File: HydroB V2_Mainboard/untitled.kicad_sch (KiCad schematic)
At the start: 12 parts, among them J3 PH SENSOR, J4 EC SENSOR, U2 SN65HVD72DR

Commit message: Mainboard schematic update
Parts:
- removed D2, D3: LED_Small, LED_SMD:LED_0805_2012Metric, symbol Device:LED_Small
- removed J4: EC SENSOR, Connector_Phoenix_MC:PhoenixContact_MCV_1,5_4-G-3.81_1x04_P3.81mm_Vertical, symbol Connector:Conn_01x04_Pin
- removed R6, R7: 1k, Resistor_SMD:R_0603_1608Metric, symbol Device:R
- added D4: D_TVS, Diode_SMD:D_SOD-123F, symbol Device:D_TVS
- added J1: Conn_01x02_Pin, DC Conn:Modbus, symbol Connector:Conn_01x02_Pin
- added J9: SENSOR, DC Conn:Modbus, symbol Connector:Conn_01x04_Pin
- added TP1, TP2: TestPoint, TestPoint:TestPoint_Loop_D1.80mm_Drill1.0mm_Beaded, symbol Connector:TestPoint
- J3: value PH SENSOR -> SENSOR; footprint Connector_Phoenix_MC:PhoenixContact_MCV_1,5_4-G-3.81_1x04_P3.81mm_Vertical -> DC Conn:Modbus
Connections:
- net +12V: now also J9.4 (Pin_4)
- net GND: now also J9.1 (Pin_1)
- net at R10.2, R11.1, R9.1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: now also J3.3 (Pin_3), D4.1 (A1), J1.1 (Pin_1), J9.3 (Pin_3), TP2.1; no longer J3.2 (Pin_2)
- net at R11.2, R8.1, R9.2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: now also J3.2 (Pin_2), D4.2 (A2), J1.2 (Pin_2), J9.2 (Pin_2), TP1.1; no longer J3.3 (Pin_3)

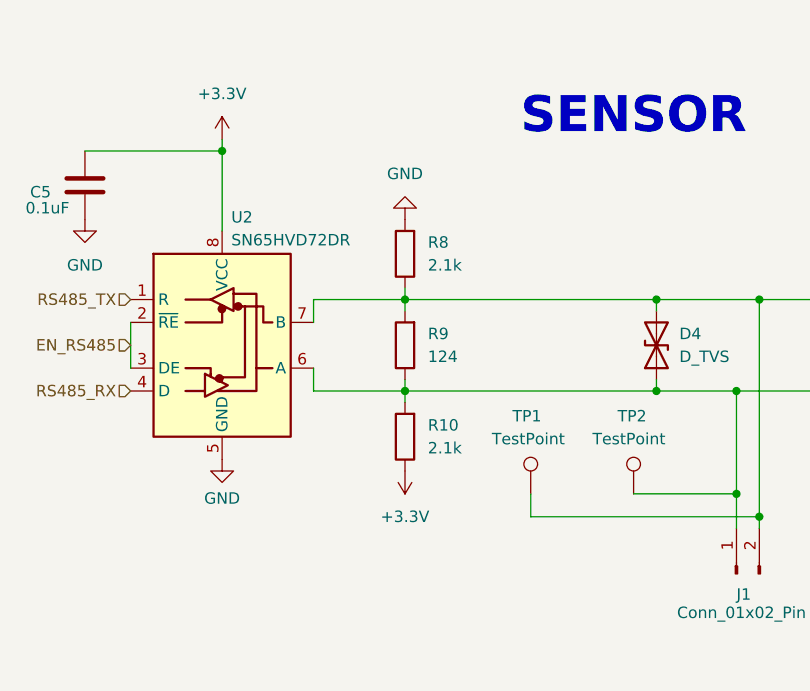
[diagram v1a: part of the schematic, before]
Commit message: main PCB board placement
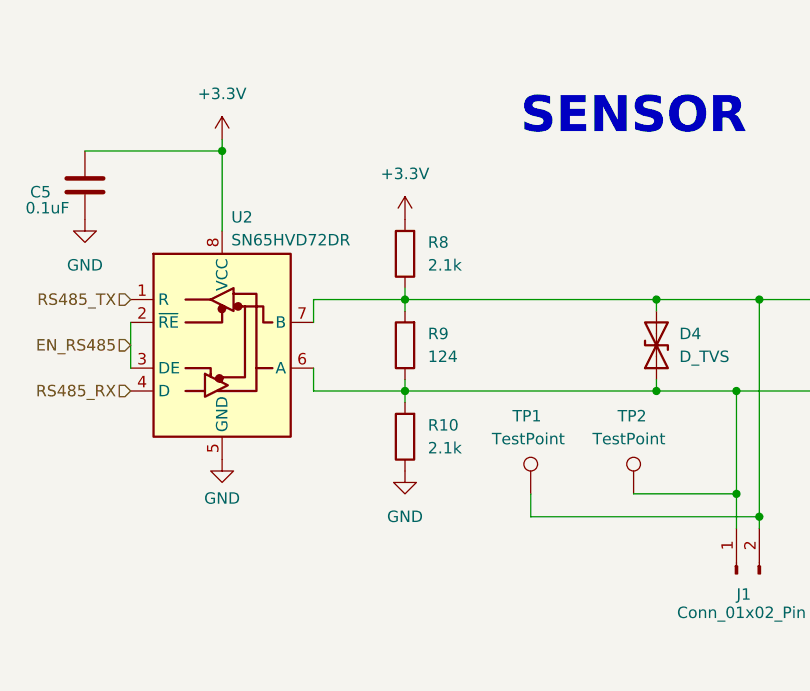
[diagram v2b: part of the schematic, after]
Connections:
- net +3.3V: now also R8.2; no longer R10.1
- net GND: now also R10.1; no longer R8.2
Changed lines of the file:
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@@
 	(symbol
 		(lib_id "power:GND")
-		(at 130.81 85.09 180)
+		(at 130.81 113.03 0)
 		(unit 1)
 		(exclude_from_sim no)
@@
 		(fields_autoplaced yes)
 		(property "Reference" "#PWR017"
-			(at 130.81 78.74 0)
+			(at 130.81 119.38 0)
 			(effects
 				(font
@@
 		)
 		(property "Value" "GND"
-			(at 130.81 80.01 0)
+			(at 130.81 118.11 0)
 			(effects
 				(font
@@
 		)
 		(property "Footprint" ""
-			(at 130.81 85.09 0)
+			(at 130.81 113.03 0)
 			(effects
 				(font
@@
 		)
 		(property "Datasheet" ""
-			(at 130.81 85.09 0)
+			(at 130.81 113.03 0)
 			(effects
 				(font
@@
 		)
 		(property "Description" "Power symbol creates a global label with name \"GND\" , ground"
-			(at 130.81 85.09 0)
+			(at 130.81 113.03 0)
 			(effects
 				(font
@@
 	(symbol
 		(lib_id "power:+3.3V")
-		(at 130.81 113.03 180)
+		(at 130.81 85.09 0)
 		(unit 1)
 		(exclude_from_sim no)
@@
 		(fields_autoplaced yes)
 		(property "Reference" "#PWR018"
-			(at 130.81 109.22 0)
+			(at 130.81 88.9 0)
 			(effects
 				(font
@@
 		)
 		(property "Value" "+3.3V"
-			(at 130.81 118.11 0)
+			(at 130.81 80.01 0)
 			(effects
 				(font
@@
 		)
 		(property "Footprint" ""
-			(at 130.81 113.03 0)
+			(at 130.81 85.09 0)
 			(effects
 				(font
@@
 		)
 		(property "Datasheet" ""
-			(at 130.81 113.03 0)
+			(at 130.81 85.09 0)
 			(effects
 				(font
@@
 		)
 		(property "Description" "Power symbol creates a global label with name \"+3.3V\""
-			(at 130.81 113.03 0)
-			(effects
-				(font
+			(at 130.81 85.09 0)
+			(effects
+				(font

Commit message: PCB placement and ERC
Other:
- company: (none) -> Modbus
- title: (none) -> Prak Chilifong
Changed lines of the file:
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@@
 	(generator_version "8.0")
 	(paper "A4")
+	(title_block
+		(title "Prak Chilifong")
+		(date "2024-10-06")
+		(rev "2.0")
+		(company "Modbus")
+		(comment 1 "Mainboard PCB")
+	)
 	(junction
 		(at 182.88 104.14)
@@
 	)
 	(junction
+		(at 201.93 118.11)
+		(diameter 0)
+		(color 0 0 0 0)
+	)
+	(junction
 		(at 170.18 118.11)
 		(diameter 0)
@@
 	(wire
 		(pts
-			(xy 201.93 115.57) (xy 201.93 119.38)
+			(xy 201.93 115.57) (xy 201.93 118.11)
 		)
 		(stroke
@@
 	(wire
 		(pts
+			(xy 201.93 118.11) (xy 201.93 119.38)
+		)
+		(stroke
+			(width 0)
+			(type default)
+		)
+	)
+	(wire
+		(pts
 			(xy 130.81 92.71) (xy 130.81 93.98)
 		)
@@
 	(wire
 		(pts
+			(xy 212.09 115.57) (xy 212.09 118.11)
+		)
+		(stroke
+			(width 0)
+			(type default)
+		)
+	)
+	(wire
+		(pts
 			(xy 170.18 93.98) (xy 180.34 93.98)
 		)
@@
 	(wire
 		(pts
+			(xy 201.93 118.11) (xy 212.09 118.11)
+		)
+		(stroke
+			(width 0)
+			(type default)
+		)
+	)
+	(wire
+		(pts
 			(xy 100.33 96.52) (xy 100.33 101.6)
 		)
@@
 	(wire
 		(pts
+			(xy 185.42 115.57) (xy 185.42 119.38)
+		)
+		(stroke
+			(width 0)
+			(type default)
+		)
+	)
+	(wire
+		(pts
 			(xy 199.39 104.14) (xy 199.39 119.38)
 		)
@@
 		(pts
 			(xy 158.75 102.87) (xy 158.75 104.14)
-		)
-		(stroke
-			(width 0)
-			(type default)
-		)
-	)
-	(wire
-		(pts
-			(xy 185.42 119.38) (xy 185.42 115.57)
 		)
 		(stroke
@@
 	(text "SENSOR\n"
 		(exclude_from_sim no)
-		(at 156.21 73.66 0)
+		(at 151.384 41.91 0)
 		(effects
 			(font
@@
 	)
 	(symbol
+		(lib_id "power:+12V")
+		(at 201.93 115.57 0)
+		(unit 1)
+		(exclude_from_sim no)
+		(in_bom yes)
+		(on_board yes)
+		(dnp no)
+		(property "Reference" "#PWR025"
+			(at 201.93 119.38 0)
+			(effects
+				(font
+					(size 1.27 1.27)
+				)
+				(hide yes)
+			)
+		)
+		(property "Value" "+12V"
+			(at 201.93 111.506 0)
+			(effects
+				(font
+					(size 1.27 1.27)
+				)
+			)
+		)
+		(property "Footprint" ""
+			(at 201.93 115.57 0)
+			(effects
+				(font
+					(size 1.27 1.27)
+				)
+				(hide yes)
+			)
+		)
+		(property "Datasheet" ""
+			(at 201.93 115.57 0)
+			(effects
+				(font
+					(size 1.27 1.27)
+				)
+				(hide yes)
+			)
+		)
+		(property "Description" "Power symbol creates a global label with name \"+12V\""
+			(at 201.93 115.57 0)
+			(effects
+				(font
+					(size 1.27 1.27)
+				)
+				(hide yes)
+			)
+		)
+		(pin "1"
+		)
+		(instances
+			(project "LCD High Revolution"
+				(path "/7eaed49e-949c-4b32-bb59-42041e199453/cb3a589e-3872-4cde-9770-3d39d4934022/02fbcb66-5250-4d03-96d3-712f7ba2e5b8"
+					(reference "#PWR025")
+					(unit 1)
+				)
+			)
+		)
+	)
+	(symbol
+		(lib_id "power:+12V")
+		(at 185.42 115.57 0)
+		(unit 1)
+		(exclude_from_sim no)
+		(in_bom yes)
+		(on_board yes)
+		(dnp no)
+		(property "Reference" "#PWR020"
+			(at 185.42 119.38 0)
+			(effects
+				(font
+					(size 1.27 1.27)
+				)
+				(hide yes)
+			)
+		)
+		(property "Value" "+12V"
+			(at 185.42 111.76 0)
+			(effects
+				(font
+					(size 1.27 1.27)
+				)
+			)
+		)
+		(property "Footprint" ""
+			(at 185.42 115.57 0)
+			(effects
+				(font
+					(size 1.27 1.27)
+				)
+				(hide yes)
+			)
+		)
+		(property "Datasheet" ""
+			(at 185.42 115.57 0)
+			(effects
+				(font
+					(size 1.27 1.27)
+				)
+				(hide yes)
+			)
+		)
+		(property "Description" "Power symbol creates a global label with name \"+12V\""
+			(at 185.42 115.57 0)
+			(effects
+				(font
+					(size 1.27 1.27)
+				)
+				(hide yes)
+			)
+		)
+		(pin "1"
+		)
+		(instances
+			(project "LCD High Revolution"
+				(path "/7eaed49e-949c-4b32-bb59-42041e199453/cb3a589e-3872-4cde-9770-3d39d4934022/02fbcb66-5250-4d03-96d3-712f7ba2e5b8"
+					(reference "#PWR020")
+					(unit 1)
+				)
+			)
+		)
+	)
+	(symbol
 		(lib_id "Device:R")
 		(at 130.81 99.06 180)
@@
 	)
 	(symbol
-		(lib_id "power:+12V")
-		(at 185.42 115.57 0)
+		(lib_id "power:PWR_FLAG")
+		(at 212.09 115.57 0)
 		(unit 1)
 		(exclude_from_sim no)
@@
 		(on_board yes)
 		(dnp no)
-		(property "Reference" "#PWR020"
-			(at 185.42 119.38 0)
-			(effects
-				(font
-					(size 1.27 1.27)
-				)
-				(hide yes)
-			)
-		)
-		(property "Value" "+12V"
-			(at 185.42 111.76 0)
+		(fields_autoplaced yes)
+		(property "Reference" "#FLG03"
+			(at 212.09 113.665 0)
+			(effects
+				(font
+					(size 1.27 1.27)
+				)
+				(hide yes)
+			)
+		)
+		(property "Value" "PWR_FLAG"
+			(at 212.09 110.49 0)
 			(effects
 				(font
@@
 		)
 		(property "Footprint" ""
-			(at 185.42 115.57 0)
-			(effects
-				(font
-					(size 1.27 1.27)
-				)
-				(hide yes)
-			)
-		)
-		(property "Datasheet" ""
-			(at 185.42 115.57 0)
-			(effects
-				(font
-					(size 1.27 1.27)
-				)
-				(hide yes)
-			)
-		)
-		(property "Description" "Power symbol creates a global label with name \"+12V\""
-			(at 185.42 115.57 0)
+			(at 212.09 115.57 0)
+			(effects
+				(font
+					(size 1.27 1.27)
+				)
+				(hide yes)
+			)
+		)
+		(property "Datasheet" "~"
+			(at 212.09 115.57 0)
+			(effects
+				(font
+					(size 1.27 1.27)
+				)
+				(hide yes)
+			)
+		)
+		(property "Description" "Special symbol for telling ERC where power comes from"
+			(at 212.09 115.57 0)
 			(effects
 				(font
@@
 			(project "LCD High Revolution"
 				(path "/7eaed49e-949c-4b32-bb59-42041e199453/cb3a589e-3872-4cde-9770-3d39d4934022/02fbcb66-5250-4d03-96d3-712f7ba2e5b8"
-					(reference "#PWR020")
+					(reference "#FLG03")
 					(unit 1)
 				)
@@
 					(unit 1)
 				)
-			)
-		)
-	)
-	(symbol
-		(lib_id "power:+12V")
-		(at 201.93 115.57 0)
-		(unit 1)
-		(exclude_from_sim no)
-		(in_bom yes)
-		(on_board yes)
-		(dnp no)
-		(property "Reference" "#PWR025"
-			(at 201.93 119.38 0)
-			(effects
-				(font
-					(size 1.27 1.27)
-				)
-				(hide yes)
-			)
-		)
-		(property "Value" "+12V"
-			(at 201.93 111.76 0)
-			(effects
-				(font
-					(size 1.27 1.27)
-				)
-			)
-		)
-		(property "Footprint" ""
-			(at 201.93 115.57 0)
-			(effects
-				(font
-					(size 1.27 1.27)
-				)
-				(hide yes)
-			)
-		)
-		(property "Datasheet" ""
-			(at 201.93 115.57 0)
-			(effects
-				(font
-					(size 1.27 1.27)
-				)
-				(hide yes)
-			)
-		)
-		(property "Description" "Power symbol creates a global label with name \"+12V\""
-			(at 201.93 115.57 0)
-			(effects
-				(font
-					(size 1.27 1.27)
-				)
-				(hide yes)
-			)
-		)
-		(pin "1"
-		)
-		(instances
-			(project "LCD High Revolution"
-				(path "/7eaed49e-949c-4b32-bb59-42041e199453/cb3a589e-3872-4cde-9770-3d39d4934022/02fbcb66-5250-4d03-96d3-712f7ba2e5b8"
-					(reference "#PWR025")
-					(unit 1)
-				)
